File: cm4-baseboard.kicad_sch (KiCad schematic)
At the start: 4 parts

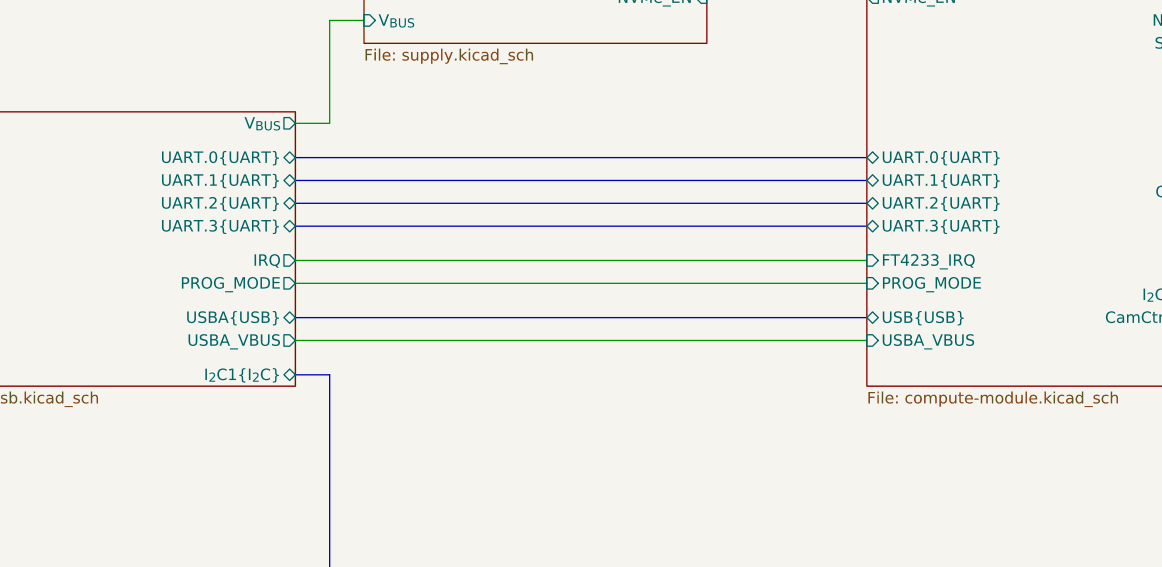
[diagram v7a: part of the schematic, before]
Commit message: [#56330] Clean ERC errors/warnings; update power supply notes
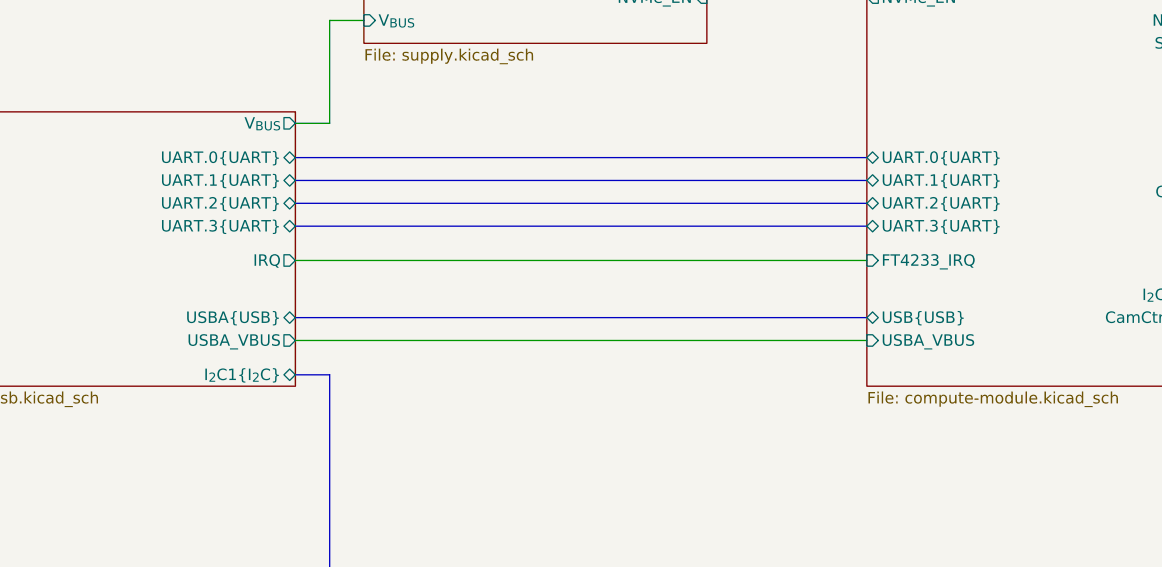
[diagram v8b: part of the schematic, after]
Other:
- sheet Compute module ports: added none; removed PROG_MODE
- sheet USB ports: added none; removed PROG_MODE
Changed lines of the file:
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@@
-    (stroke (width 0) (type default))
-  )
-  (wire (pts (xy 135.89 149.86) (xy 199.39 149.86))
     (stroke (width 0) (type default))
   )
@@
       (effects (font (size 1.27 1.27)) (justify right))
     )
-    (pin "PROG_MODE" input (at 199.39 149.86 180)
-      (effects (font (size 1.27 1.27)) (justify left))
-    )
     (pin "~{POE EN}" output (at 199.39 109.22 180)
       (effects (font (size 1.27 1.27)) (justify left))
@@
       (effects (font (size 1.27 1.27)) (justify right))
     )
-    (pin "PROG_MODE" output (at 135.89 149.86 0)
-      (effects (font (size 1.27 1.27)) (justify right))
-    )
